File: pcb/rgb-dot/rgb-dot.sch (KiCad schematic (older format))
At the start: 4 parts, among them J1 HEADER-1x03, J2 HEADER-1x03, U1 WS2812B

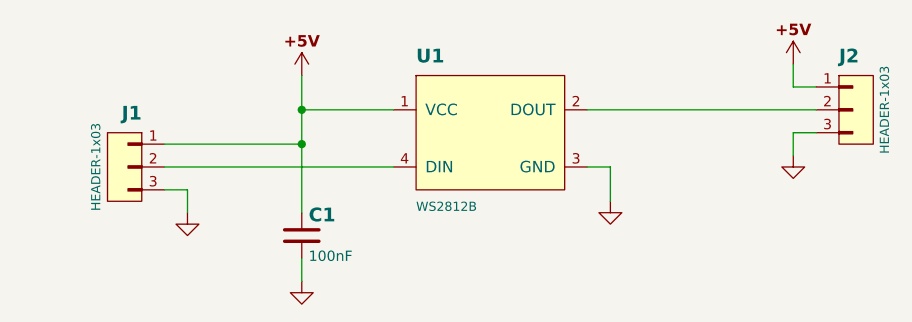
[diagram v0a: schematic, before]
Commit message: Updated PCB pc-01 pc-02, Added display base pcb (pc-03, pc-04)
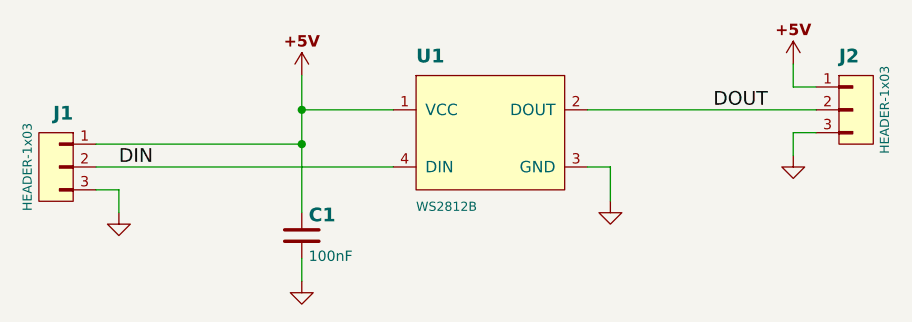
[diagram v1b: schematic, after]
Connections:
- net DOUT: now reaches J2.2 (P2), U1.2 (DOUT)
- net DIN: now reaches J1.2 (P2), U1.4 (DIN)
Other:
- moved on the sheet: J1
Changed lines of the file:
@@
 Comp ""
 Comment1 "CLKV2-PC-02"
-Comment2 "CLKV2-DWG-03"
+Comment2 "CLKV2-SCH-02"
 Comment3 "Linux alarm clock (V2)"
 Comment4 ""
@@
 L HEADER-1x03 J1
 U 1 1 5570175C
-P 4200 4300
-F 0 "J1" H 4150 4500 60  0000 L BNB
-F 1 "HEADER-1x03" V 4350 4300 40  0000 C CNN
-F 2 "Conn-Wire-Pads:WP-50mil-1x03" H 4200 4300 60  0001 C CNN
-F 3 "" H 4200 4300 60  0001 C CNN
-F 4 "-" H 4150 4600 40  0001 L BNN "Part"
-F 5 "Connector" H 4150 4700 40  0001 L BNN "Family"
-	1    4200 4300
+P 3900 4300
+F 0 "J1" H 3850 4500 60  0000 L BNB
+F 1 "HEADER-1x03" V 4050 4300 40  0000 C CNN
+F 2 "Conn-Wire-Pads:WP-50mil-1x03" H 3900 4300 60  0001 C CNN
+F 3 "" H 3900 4300 60  0001 C CNN
+F 4 "-" H 3850 4600 40  0001 L BNN "Part"
+F 5 "Connector" H 3850 4700 40  0001 L BNN "Family"
+	1    3900 4300
 	-1   0    0    -1
 $EndComp
@@
 $EndComp
 Wire Wire Line
-	5350 4300 4350 4300
+	5350 4300 4050 4300
 Wire Wire Line
 	6200 4050 7200 4050
@@
 L GND #PWR01
 U 1 1 5570198A
-P 4450 4500
-F 0 "#PWR01" H 4450 4550 30  0001 C CNN
-F 1 "GND" H 4450 4375 30  0001 C CNN
-F 2 "" H 4450 4500 60  0000 C CNN
-F 3 "" H 4450 4500 60  0000 C CNN
-	1    4450 4500
+P 4150 4500
+F 0 "#PWR01" H 4150 4550 30  0001 C CNN
+F 1 "GND" H 4150 4375 30  0001 C CNN
+F 2 "" H 4150 4500 60  0000 C CNN
+F 3 "" H 4150 4500 60  0000 C CNN
+	1    4150 4500
 	1    0    0    -1
 $EndComp
 Wire Wire Line
-	4950 4200 4350 4200
+	4950 4200 4050 4200
 Wire Wire Line
-	4350 4400 4450 4400
+	4050 4400 4150 4400
 Wire Wire Line
-	4450 4400 4450 4500
+	4150 4400 4150 4500
 Wire Wire Line
 	4950 3900 4950 4500
@@
 	4950 4700 4950 4800
 Connection ~ 4950 4200
+Text Label 4150 4300 0    60   ~ 0
+DIN
+Text Label 6750 4050 0    60   ~ 0
+DOUT
 $EndSCHEMATC
